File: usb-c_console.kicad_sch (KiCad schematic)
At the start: 0 parts

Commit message: [#56643] Create buses for interfaces, assign buses to blocks
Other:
- company: (none) -> Antmicro Ltd.
- title: (none) -> Com Express 7 baseboard
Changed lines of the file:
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@@
 (kicad_sch (version 20230121) (generator eeschema)
-  (paper "A4")
-  (bus_alias "UART" (members ))
+  (paper "A3")
+  (title_block
+    (title "Com Express 7 baseboard")
+    (date "2024-03-22")
+    (rev "1.0.0")
+    (company "Antmicro Ltd.")
+  )
+  (bus_alias "UART" (members "RX" "TX"))
   (hierarchical_label "UART{UART}" (shape bidirectional) (at 256.54 101.6 0) (fields_autoplaced)
     (effects (font (size 1.27 1.27)) (justify left))

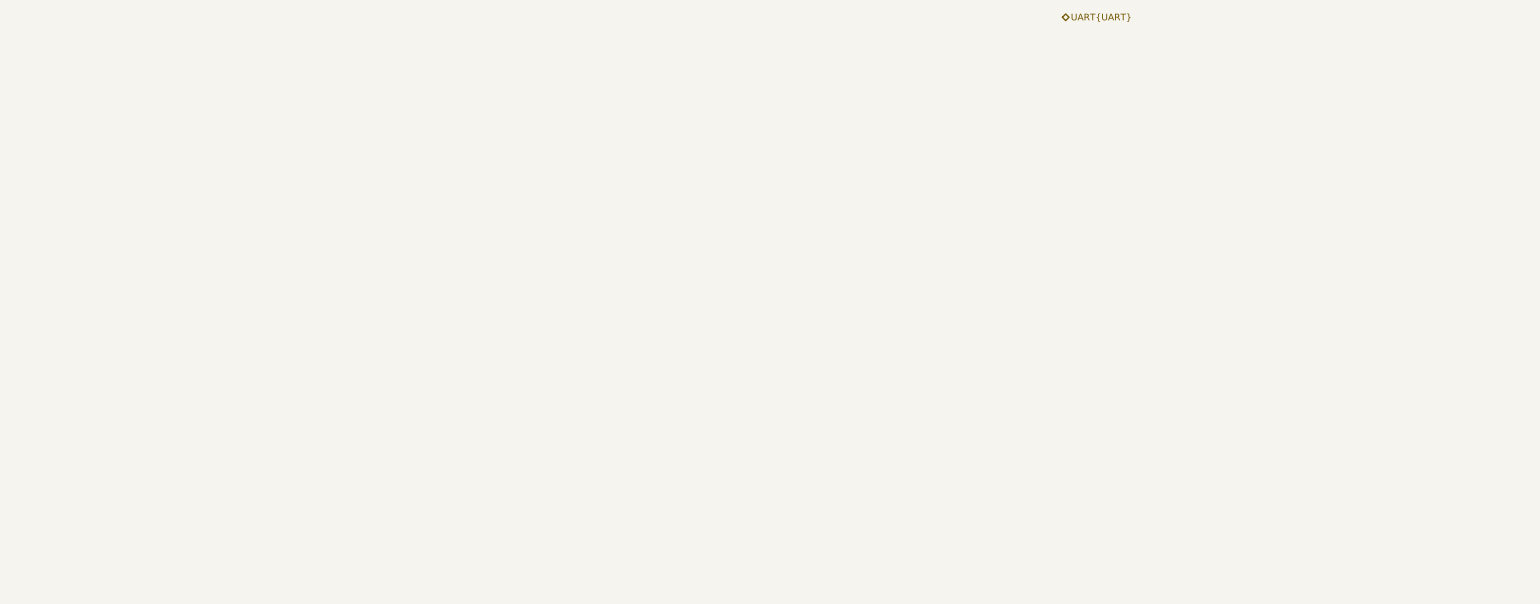
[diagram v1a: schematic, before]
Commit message: [#57056] Add USB-C console
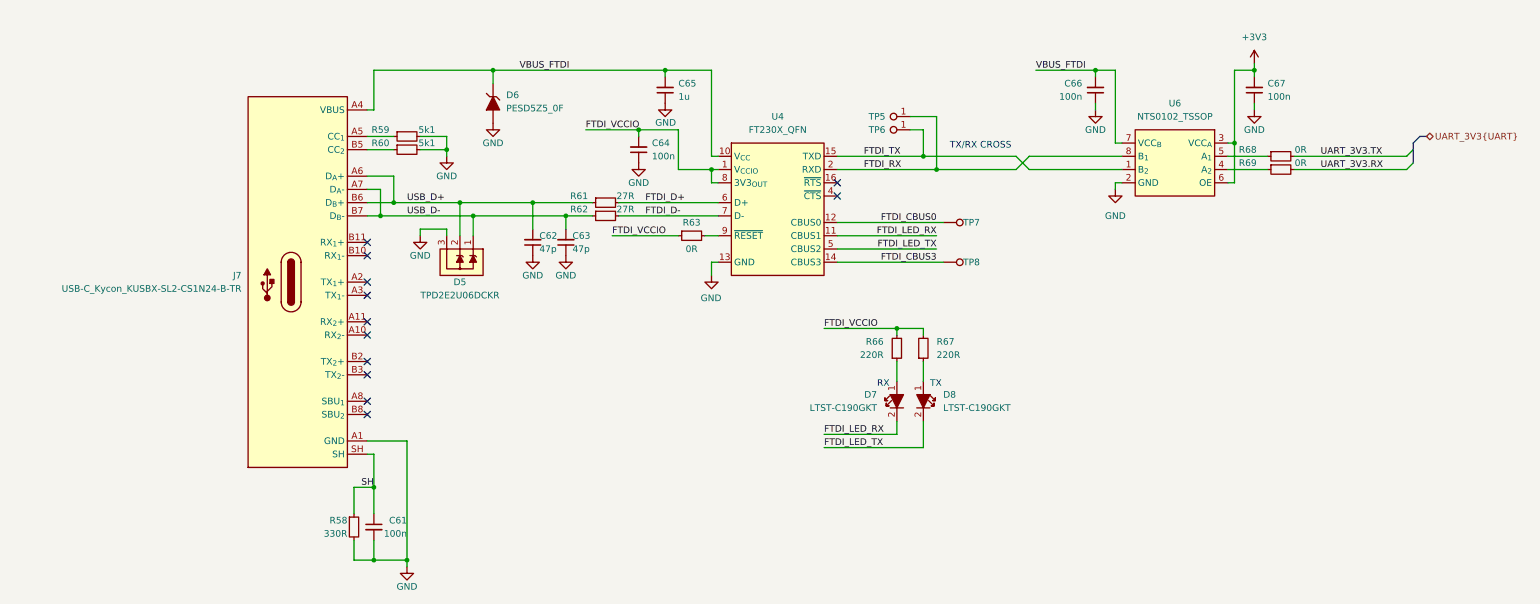
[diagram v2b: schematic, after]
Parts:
- added C61, C64, C66, C67: C_100n_0402, antmicro-footprints:C_0402_1005Metric, symbol antmicroCapacitors0402:C_100n_0402
- added C62, C63: C_47p_0402, antmicro-footprints:C_0402_1005Metric, symbol antmicroCapacitors0402:C_47p_0402
- added C65: C_1u_0402, antmicro-footprints:C_0402_1005Metric, symbol antmicroCapacitors0402:C_1u_0402
- added D5: TPD2E2U06DCKR, antmicro-footprints:SC70-3, symbol antmicroTVSDiodes:TPD2E2U06DCKR
- added D6: PESD5Z5_0F, antmicro-footprints:SOD-523, symbol antmicroTVSDiodes:PESD5Z5_0F
- added D7, D8: LED_G_0603_LTST-C190GKT, antmicro-footprints:LED_0603_1608Metric_G, symbol antmicroLEDIndicationDiscrete:LED_G_0603_LTST-C190GKT
- added J7: USB-C_Kycon_KUSBX-SL2-CS1N24-B-TR, antmicro-footprints:USB-C_Receptacle_Kycon_KUSBX-SL2-CS1N24-B-TR, symbol antmicroUSBConnectors:USB-C_Kycon_KUSBX-SL2-CS1N24-B-TR
- added R58: R_330R_0402, antmicro-footprints:R_0402_1005Metric, symbol antmicroResistors0402:R_330R_0402
- added R59, R60: R_5k1_0402, antmicro-footprints:R_0402_1005Metric, symbol antmicroResistors0402:R_5k1_0402
- added R61, R62: R_27R_0402, antmicro-footprints:R_0402_1005Metric, symbol antmicroResistors0402:R_27R_0402
- added R63, R68, R69: R_0R_0402, antmicro-footprints:R_0402_1005Metric, symbol antmicroResistors0402:R_0R_0402
- added R66, R67: R_220R_0402, antmicro-footprints:R_0402_1005Metric, symbol antmicroResistors0402:R_220R_0402
- added TP5, TP6, TP7, TP8: TP_0.75mm_SMD, antmicro-footprints:TP_SMD_0.75mm, symbol antmicroTestPoints:TP_0.75mm_SMD
- added U4: FT230X_QFN, antmicro-footprints:QFN-16-1EP_4x4mm_P0.65mm, symbol antmicroInterfaceControllers:FT230X_QFN
- added U6: NTS0102_TSSOP, antmicro-footprints:TSSOP-8_3x3mm_P0.65mm, symbol antmicroLogicTranslatorsLevelShifters:NTS0102_TSSOP
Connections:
- new net: J7.A5 (CC_{1}), R59.1
- new net: J7.B5 (CC_{2}), R60.1
- new net: R63.2, U4.9 (~{RESET})
- new net: R68.1, U6.5 (A_{1})
- new net: D7.1, R66.1
- new net: D8.1, R67.1
- new net: R69.1, U6.4 (A_{2})
- new net +3V3: C67.2, U6.3 (VCC_{A}), U6.6 (OE)
- new net FTDI_CBUS0: TP7.1, U4.12 (CBUS0)
- new net FTDI_CBUS3: TP8.1, U4.14 (CBUS3)
- new net FTDI_D+: R61.2, U4.6 (D+)
- new net FTDI_D-: R62.2, U4.7 (D-)
- new net FTDI_LED_RX: D7.2, U4.11 (CBUS1)
- new net FTDI_LED_TX: D8.2, U4.5 (CBUS2)
- new net FTDI_RX: TP5.1, U4.2 (RXD), U6.8 (B_{1})
- new net FTDI_TX: TP6.1, U4.15 (TXD), U6.1 (B_{2})
- new net FTDI_VCCIO: C64.2, R63.1, R66.2, R67.2, U4.1 (V_{CCIO}), U4.8 (3V3_{OUT})
- new net GND: C61.2, C62.1, C63.1, C64.1, C65.1, C66.1, C67.1, D5.3, D6.2, J7.A1 (GND), J7.A12 (GND), J7.B1 (GND), J7.B12 (GND), R58.2, R59.2, R60.2, U4.13 (GND), U4.17 (GND), U4.3 (GND), U6.2 (GND)
- new net SH: C61.1, J7.SH, R58.1
- new net UART_3V3.RX: R69.2
- new net UART_3V3.TX: R68.2
- new net USB_D+: C62.2, D5.2, J7.A6 (D_{A}+), J7.B6 (D_{B}+), R61.1
- new net USB_D-: C63.2, D5.1, J7.A7 (D_{A}-), J7.B7 (D_{B}-), R62.1
- new net VBUS_FTDI: C65.2, C66.2, D6.1, J7.A4 (VBUS), J7.A9 (VBUS), J7.B4 (VBUS), J7.B9 (VBUS), U4.10 (V_{CC}), U6.7 (VCC_{B})
- no-connect marks 0 -> 12
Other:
- note added: "RX"
- note added: "TX"
- note added: "TX/RX CROSS"

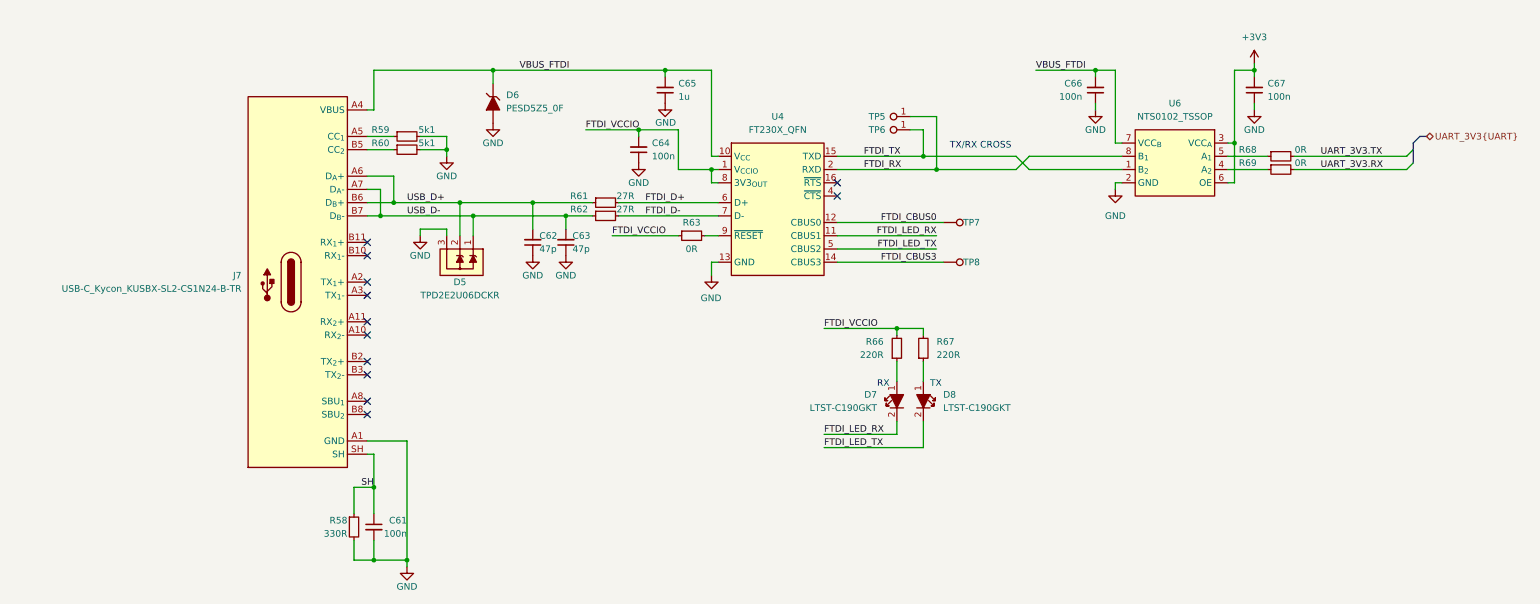
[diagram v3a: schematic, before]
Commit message: [#58137] Update backplane connector pinout
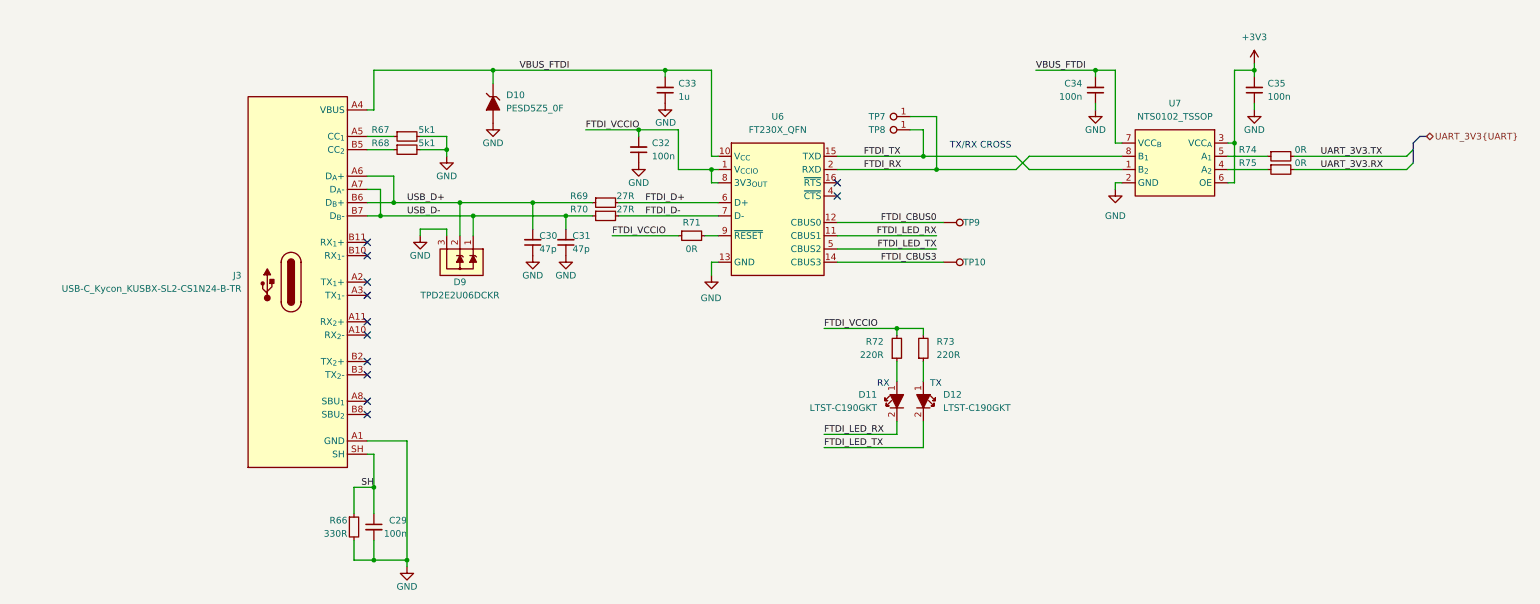
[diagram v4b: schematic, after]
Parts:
- renumbered C61 to C29, C62 to C30, C63 to C31, C64 to C32, C65 to C33, C66 to C34, C67 to C35, D6 to D10, D7 to D11, D8 to D12, D5 to D9, J7 to J3, R58 to R66, R59 to R67, R60 to R68, R61 to R69, R62 to R70, R63 to R71, R66 to R72, R67 to R73, R68 to R74, R69 to R75, TP8 to TP10, TP5 to TP7, TP6 to TP8, TP7 to TP9, U4 to U6, U6 to U7

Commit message: Fix ERC
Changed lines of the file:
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@@
   (junction (at 154.94 137.16) (diameter 0) (color 0 0 0 0)
+  )
+  (junction (at 124.46 111.76) (diameter 0) (color 0 0 0 0)
   )
   (junction (at 140.97 137.16) (diameter 0) (color 0 0 0 0)
@@
   )
   (wire (pts (xy 229.87 161.29) (xy 229.87 162.56))
+    (stroke (width 0) (type default))
+  )
+  (wire (pts (xy 123.19 111.76) (xy 124.46 111.76))
     (stroke (width 0) (type default))
   )
@@
     )
   )
+  (symbol (lib_id "antmicropower:PWR_FLAG") (at 123.19 111.76 90) (unit 1)
+    (in_bom yes) (on_board yes) (dnp no) (fields_autoplaced)
+    (property "Reference" "#FLG012" (at 121.285 111.76 0)
+      (effects (font (size 1.27 1.27)) hide)
+    )
+    (property "Value" "PWR_FLAG" (at 119.38 111.7599 90)
+      (effects (font (size 1.27 1.27)) (justify left))
+    )
+    (property "Footprint" "" (at 123.19 111.76 0)
+      (effects (font (size 1.27 1.27)) hide)
+    )
+    (property "Datasheet" "" (at 123.19 111.76 0)
+      (effects (font (size 1.27 1.27)) hide)
+    )
+    (pin "1")
+    (instances
+      (project "com-express-7-baseboard"
+        (path "/1b8c34da-dad5-4b0b-8c4b-45db766c4dfa/443bd4b5-8a40-4669-9915-56b6f474530f"
+          (reference "#FLG012") (unit 1)
+        )
+      )
+    )
+  )
   (symbol (lib_id "antmicroResistors0402:R_220R_0402") (at 229.87 167.64 90) (unit 1)
     (in_bom yes) (on_board yes) (dnp no) (fields_autoplaced)
@@
         )
       )
+    )
+  )
+  (symbol (lib_id "antmicropower:PWR_FLAG") (at 165.1 123.19 90) (unit 1)
+    (in_bom yes) (on_board yes) (dnp no) (fields_autoplaced)
+    (property "Reference" "#FLG09" (at 163.195 123.19 0)
+      (effects (font (size 1.27 1.27)) hide)
+    )
+    (property "Value" "PWR_FLAG" (at 161.29 123.1899 90)
+      (effects (font (size 1.27 1.27)) (justify left))
+    )
+    (property "Footprint" "" (at 165.1 123.19 0)
+      (effects (font (size 1.27 1.27)) hide)
+    )
+    (property "Datasheet" "" (at 165.1 123.19 0)
+      (effects (font (size 1.27 1.27)) hide)
+    )
+    (pin "1")
+    (instances
+      (project "com-express-7-baseboard"
+        (path "/1b8c34da-dad5-4b0b-8c4b-45db766c4dfa/443bd4b5-8a40-4669-9915-56b6f474530f"
+          (reference "#FLG09") (unit 1)
+        )
+      )

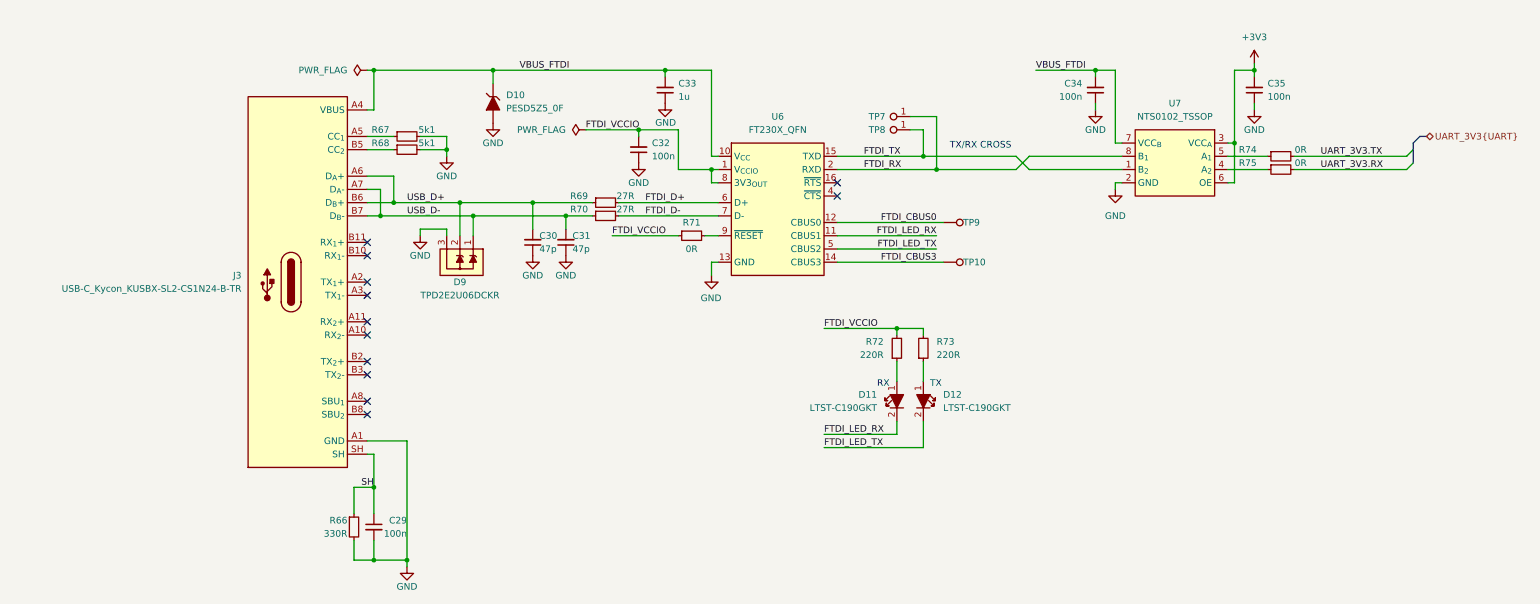
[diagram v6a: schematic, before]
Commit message: Update components from the library
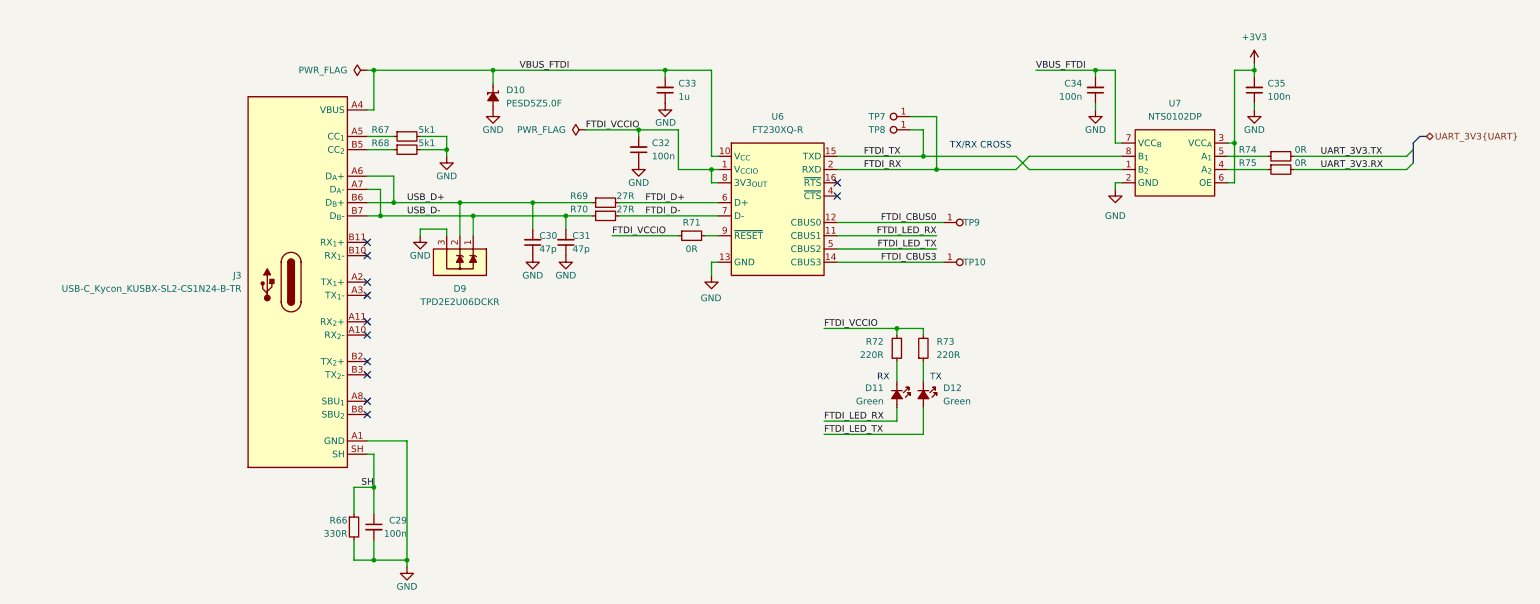
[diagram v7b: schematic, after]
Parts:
- removed D9: TPD2E2U06DCKR, antmicro-footprints:SC70-3, symbol antmicroTVSDiodes:TPD2E2U06DCKR
- added D9: TPD2E2U06_SC70, antmicro-footprints:SC70-3, symbol antmicroTVSDiodes:TPD2E2U06_SC70
- C29, C30, C31, C32, C33, C34, C35, D10, R66, R67, R68, R69, R70, R71, R72, R73, R74, R75: Public (none) -> False
- D11, D12: Color (none) -> Green; Manufacturer Lite-On Inc. -> Lite-On; Public (none) -> False
- TP10, TP7, TP8, TP9: Public (none) -> False; now left out of the parts list
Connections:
- net GND: now also D9.3
- net USB_D+: now also D9.2
- net USB_D-: now also D9.1
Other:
- moved on the sheet: D11, D12
